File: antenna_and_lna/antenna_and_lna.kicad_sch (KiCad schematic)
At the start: 9 parts, among them J1 CON-SMA-EDGE-S, J2 TSW-104-14-F-S

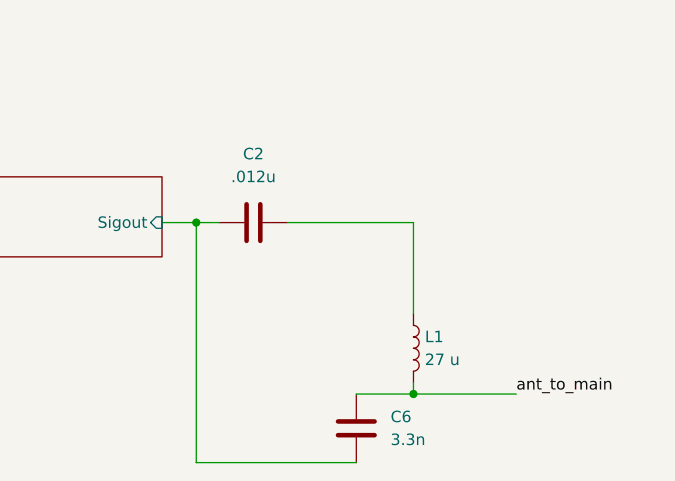
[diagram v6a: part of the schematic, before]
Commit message: Fixed edge clearance for both boards, both DRC clean
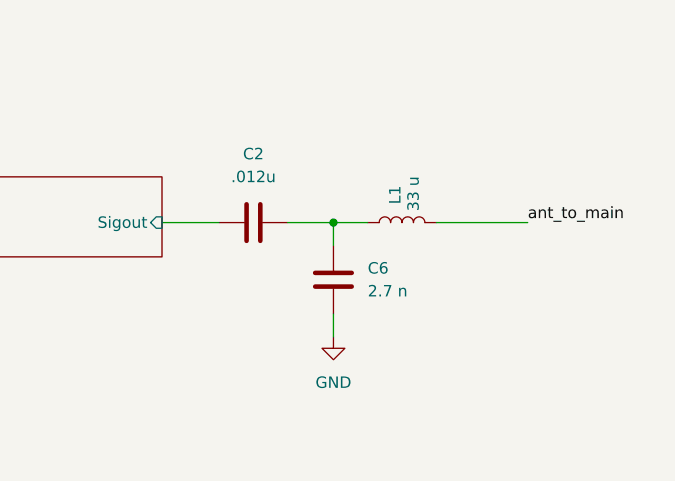
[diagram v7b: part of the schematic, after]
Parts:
- C6: value 3.3n -> 2.7 n
- L1: value 27 u -> 33 u
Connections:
- net GND: now also C6.2
- net LNA/Sigout: no longer C6.2
- net ant_to_main: no longer C6.1
- net at C2.2, L1.1: now also C6.1
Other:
- moved on the sheet: C6, L1
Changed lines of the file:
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@@
 	)
 	(junction
-		(at 218.44 101.6)
+		(at 233.68 101.6)
 		(diameter 0)
 		(color 0 0 0 0)
@@
 		(color 0 0 0 0)
 	)
-	(junction
-		(at 242.57 120.65)
-		(diameter 0)
-		(color 0 0 0 0)
-	)
 	(wire
 		(pts
@@
 	(wire
 		(pts
-			(xy 218.44 128.27) (xy 218.44 101.6)
-		)
-		(stroke
-			(width 0)
-			(type default)
-		)
-	)
-	(wire
-		(pts
 			(xy 49.53 90.17) (xy 62.23 90.17)
 		)
@@
 	(wire
 		(pts
-			(xy 218.44 101.6) (xy 220.98 101.6)
+			(xy 214.63 101.6) (xy 220.98 101.6)
 		)
 		(stroke
@@
 	(wire
 		(pts
-			(xy 236.22 128.27) (xy 218.44 128.27)
-		)
-		(stroke
-			(width 0)
-			(type default)
-		)
-	)
-	(wire
-		(pts
-			(xy 228.6 101.6) (xy 242.57 101.6)
-		)
-		(stroke
-			(width 0)
-			(type default)
-		)
-	)
-	(wire
-		(pts
-			(xy 242.57 120.65) (xy 242.57 119.38)
+			(xy 228.6 101.6) (xy 233.68 101.6)
+		)
+		(stroke
+			(width 0)
+			(type default)
+		)
+	)
+	(wire
+		(pts
+			(xy 245.11 101.6) (xy 255.27 101.6)
 		)
 		(stroke
@@
 	(wire
 		(pts
+			(xy 233.68 101.6) (xy 237.49 101.6)
+		)
+		(stroke
+			(width 0)
+			(type default)
+		)
+	)
+	(wire
+		(pts
 			(xy 116.84 80.01) (xy 116.84 85.09)
 		)
@@
 	(wire
 		(pts
-			(xy 214.63 101.6) (xy 218.44 101.6)
-		)
-		(stroke
-			(width 0)
-			(type default)
-		)
-	)
-	(wire
-		(pts
-			(xy 242.57 101.6) (xy 242.57 111.76)
+			(xy 233.68 101.6) (xy 233.68 104.14)
+		)
+		(stroke
+			(width 0)
+			(type default)
+		)
+	)
+	(wire
+		(pts
+			(xy 233.68 111.76) (xy 233.68 114.3)
 		)
 		(stroke
@@
 	(wire
 		(pts
-			(xy 242.57 120.65) (xy 254 120.65)
-		)
-		(stroke
-			(width 0)
-			(type default)
-		)
-	)
-	(wire
-		(pts
 			(xy 110.49 74.93) (xy 110.49 77.47)
 		)
@@
 		(pts
 			(xy 116.84 85.09) (xy 120.65 85.09)
-		)
-		(stroke
-			(width 0)
-			(type default)
-		)
-	)
-	(wire
-		(pts
-			(xy 236.22 120.65) (xy 242.57 120.65)
 		)
 		(stroke
@@
 	)
 	(label "ant_to_main"
-		(at 254 120.65 0)
+		(at 255.27 101.6 0)
 		(effects
 			(font
@@
 	(symbol
 		(lib_id "Device:C")
-		(at 236.22 124.46 0)
+		(at 233.68 107.95 0)
 		(unit 1)
 		(exclude_from_sim no)
@@
 		(fields_autoplaced yes)
 		(property "Reference" "C6"
-			(at 240.03 123.1899 0)
+			(at 237.49 106.6799 0)
 			(effects
 				(font
@@
 			)
 		)
-		(property "Value" "3.3n"
-			(at 240.03 125.7299 0)
+		(property "Value" "2.7 n"
+			(at 237.49 109.2199 0)
 			(effects
 				(font
@@
 		)
 		(property "Footprint" "Capacitor_SMD:C_0603_1608Metric"
-			(at 237.1852 128.27 0)
+			(at 234.6452 111.76 0)
 			(effects
 				(font
@@
 		)
 		(property "Datasheet" "~"
-			(at 236.22 124.46 0)
+			(at 233.68 107.95 0)
 			(effects
 				(font
@@
 		)
 		(property "Description" "Unpolarized capacitor"
-			(at 236.22 124.46 0)
+			(at 233.68 107.95 0)
 			(effects
 				(font
@@
 	(symbol
 		(lib_id "Device:L")
-		(at 242.57 115.57 0)
-		(unit 1)
-		(exclude_from_sim no)
-		(in_bom yes)
-		(on_board yes)
-		(dnp no)
-		(fields_autoplaced yes)
+		(at 241.3 101.6 90)
+		(unit 1)
+		(exclude_from_sim no)
+		(in_bom yes)
+		(on_board yes)
+		(dnp no)
 		(property "Reference" "L1"
-			(at 243.84 114.2999 0)
+			(at 240.538 99.568 0)
 			(effects
 				(font
@@
 			)
 		)
-		(property "Value" "27 u"
-			(at 243.84 116.8399 0)
+		(property "Value" "33 u"
+			(at 242.5699 100.33 0)
 			(effects
 				(font
@@
 		)
 		(property "Footprint" "Inductor_SMD:L_0603_1608Metric"
-			(at 242.57 115.57 0)
+			(at 241.3 101.6 0)
 			(effects
 				(font
@@
 		)
 		(property "Datasheet" "~"
-			(at 242.57 115.57 0)
+			(at 241.3 101.6 0)
 			(effects
 				(font
@@
 		)
 		(property "Description" "Inductor"
-			(at 242.57 115.57 0)
+			(at 241.3 101.6 0)
 			(effects
 				(font
@@
 					(unit 1)
 				)
+			)
+		)
+	)
+	(symbol
+		(lib_id "power:GND")
+		(at 233.68 114.3 0)
+		(unit 1)
+		(exclude_from_sim no)
+		(in_bom yes)
+		(on_board yes)
+		(dnp no)
+		(fields_autoplaced yes)
+		(property "Reference" "#PWR014"
+			(at 233.68 120.65 0)
+			(effects
+				(font
+					(size 1.27 1.27)
+				)
+				(hide yes)
+			)
+		)
+		(property "Value" "GND"
+			(at 233.68 119.38 0)
+			(effects
+				(font
+					(size 1.27 1.27)
+				)
+			)
+		)
+		(property "Footprint" ""
+			(at 233.68 114.3 0)
+			(effects
+				(font
+					(size 1.27 1.27)
+				)
+				(hide yes)
+			)
+		)
+		(property "Datasheet" ""
+			(at 233.68 114.3 0)
+			(effects
+				(font
+					(size 1.27 1.27)
+				)
+				(hide yes)
+			)
+		)
+		(property "Description" "Power symbol creates a global label with name \"GND\" , ground"
+			(at 233.68 114.3 0)
+			(effects
+				(font
+					(size 1.27 1.27)
+				)
+				(hide yes)
+			)
+		)
+		(pin "1"
+		)
+		(instances
+			(project ""
+				(path "/c07072f1-c9e3-48f9-9b82-810fab6a13ee"
+					(reference "#PWR014")
+					(unit 1)
+				)
